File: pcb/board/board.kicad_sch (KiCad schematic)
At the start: 31 parts, among them J1 USB_C_Receptacle_USB2.0_14P, J2 Conn_01x03, SW1 SW_Push, U1 RP2040, U2 NCP1117-3.3_SOT223, U3 W25Q128JVS, Y1 12MHz

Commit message: 08012026 - tons of schematic work!
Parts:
- added C18, C19: 10uF, symbol Device:C
- added C20, C25: 1uF, symbol Device:C
- added C21, C22: 15uF, symbol Device:C
- added C23, C24, C26, C27, C28, C29, C30, C31, C32, C33, C34: 0.1uF, symbol Device:C
- added D1, D2: D, symbol Device:D
- added J3: (B) USB_C_Receptacle_USB2.0_14P, symbol Connector:USB_C_Receptacle_USB2.0_14P
- added J4: (C) USB_C_Receptacle_USB2.0_14P, symbol Connector:USB_C_Receptacle_USB2.0_14P
- added J5: Conn_01x03, symbol Connector_Generic:Conn_01x03
- added R10, R11, R8, R9: 5.1K, symbol Device:R
- added R12, R13: 27, symbol Device:R
- added R14, R16: 1K, symbol Device:R
- added R15: 10K, symbol Device:R
- added SW2: SW_Push, symbol Switch:SW_Push
- added U4: NCP1117-3.3_SOT223, Package_TO_SOT_SMD:SOT-223-3_TabPin2, symbol Regulator_Linear:NCP1117-3.3_SOT223
- added U5: RP2040, Package_DFN_QFN:QFN-56-1EP_7x7mm_P0.4mm_EP3.2x3.2mm, symbol MCU_RaspberryPi:RP2040
- added U6: W25Q128JVS, Package_SO:SOIC-8_5.23x5.23mm_P1.27mm, symbol Memory_Flash:W25Q128JVS
- added Y2: 12MHz, symbol Device:Crystal_GND24
- J1: value USB_C_Receptacle_USB2.0_14P -> (A) USB_C_Receptacle_USB2.0_14P
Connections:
- net GND: now also C18.2, C19.2, C20.2, C21.1, C22.1, C23.2, C24.2, C25.2, C26.2, C27.2, C28.2, C29.2, C30.2, C31.2, C32.2, C33.2, C34.2, J3.A1 (GND), J3.A12 (GND), J3.B1 (GND), J3.B12 (GND), J3.S1 (SHIELD), J4.A1 (GND), J4.A12 (GND), J4.B1 (GND), J4.B12 (GND), J4.S1 (SHIELD), J5.2 (Pin_2), R10.2, R11.1, R8.2, R9.1, SW2.1, U4.1 (GND), U5.19 (TESTEN), U5.57 (GND), U6.4 (GND), Y2.2, Y2.4
- net +1V1 renamed +1V1_A
- net +3V3 renamed +3V3_A
- net QSPI_SCLK renamed QSPI_SCLK_A
- net QSPI_SD0 renamed QSPI_SD0_A
- net QSPI_SD1 renamed QSPI_SD1_A
- net QSPI_SD2 renamed QSPI_SD2_A
- net QSPI_SD3 renamed QSPI_SD3_A
- net QSPI_SS renamed QSPI_SS_A
- net RUN renamed RUN_A
- net SWCLK renamed SWCLK_A
- net SWD renamed SWD_A
- net USB D+ renamed USB_A D+
- net USB D- renamed USB_A D-
- net VBUS renamed VBUS_A
- net VBUS_A: now also D1.1 (K)
- net XIN renamed XIN_A
- net XOUT renamed XOUT_A
- new net: D1.2 (A), D2.2 (A), J4.A4 (VBUS), J4.A9 (VBUS), J4.B4 (VBUS), J4.B9 (VBUS)
- new net: C22.2, R16.1, Y2.1
- new net: J4.A5 (CC1), R10.1
- new net: J4.B5 (CC2), R11.2
- new net: R14.1, SW2.2
- new net: J3.A5 (CC1), R8.1
- new net: R13.1, U5.46 (USB_DM)
- new net: R12.2, U5.47 (USB_DP)
- new net: J3.B5 (CC2), R9.2
- new net +1V1_B: C20.1, C23.1, C24.1, U5.23 (DVDD), U5.45 (VREG_VOUT), U5.50 (DVDD)
- new net +3V3_B: C19.1, C25.1, C26.1, C27.1, C28.1, C29.1, C30.1, C31.1, C32.1, C33.1, C34.1, R15.1, U4.2 (VO), U5.1 (IOVDD), U5.10 (IOVDD), U5.22 (IOVDD), U5.33 (IOVDD), U5.42 (IOVDD), U5.43 (ADC_AVDD), U5.44 (VREG_IN), U5.48 (USB_VDD), U5.49 (IOVDD), U6.8 (VCC)
- new net QSPI_SCLK_B: U5.52 (QSPI_SCLK), U6.6 (CLK)
- new net QSPI_SD0_B: U5.53 (QSPI_SD0), U6.5 (DI(IO0))
- new net QSPI_SD1_B: U5.55 (QSPI_SD1), U6.2 (DO(IO1))
- new net QSPI_SD2_B: U5.54 (QSPI_SD2), U6.3 (IO2)
- new net QSPI_SD3_B: U5.51 (QSPI_SD3), U6.7 (IO3)
- new net QSPI_SS_B: R14.2, R15.2, U5.56 (QSPI_SS), U6.1 (~{CS})
- new net RUN_B: U5.26 (RUN)
- new net SWCLK_B: J5.1 (Pin_1), U5.24 (SWCLK)
- new net SWD_B: J5.3 (Pin_3), U5.25 (SWD)
- new net USB_B D+: J3.A6 (D+), J3.B6 (D+), R12.1
- new net USB_B D-: J3.A7 (D-), J3.B7 (D-), R13.2
- new net VBUS_B: C18.1, D2.1 (K), J3.A4 (VBUS), J3.A9 (VBUS), J3.B4 (VBUS), J3.B9 (VBUS), U4.3 (VI)
- new net XIN_B: C21.2, U5.20 (XIN), Y2.3
- new net XOUT_B: R16.2, U5.21 (XOUT)
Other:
- note added: "TODO: NEED TO SELECT DIODES!!!"
- moved on the sheet: C1, C10, C11, C12, C13, C14, C15, C16, C17, C2, C3, C4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

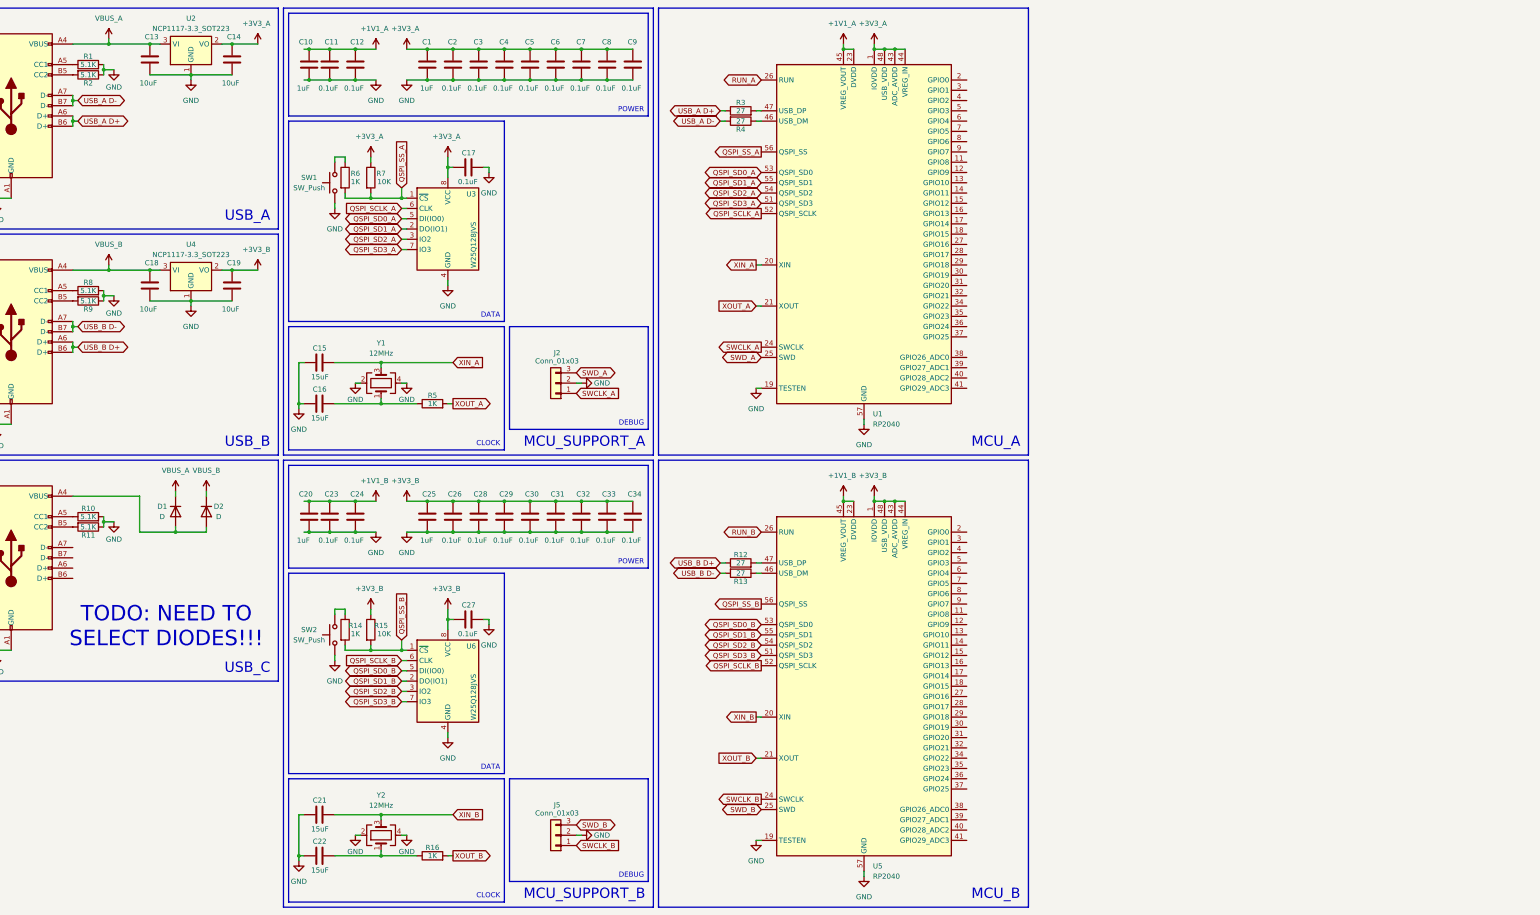
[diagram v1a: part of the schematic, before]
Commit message: add connector pins to the schematic!
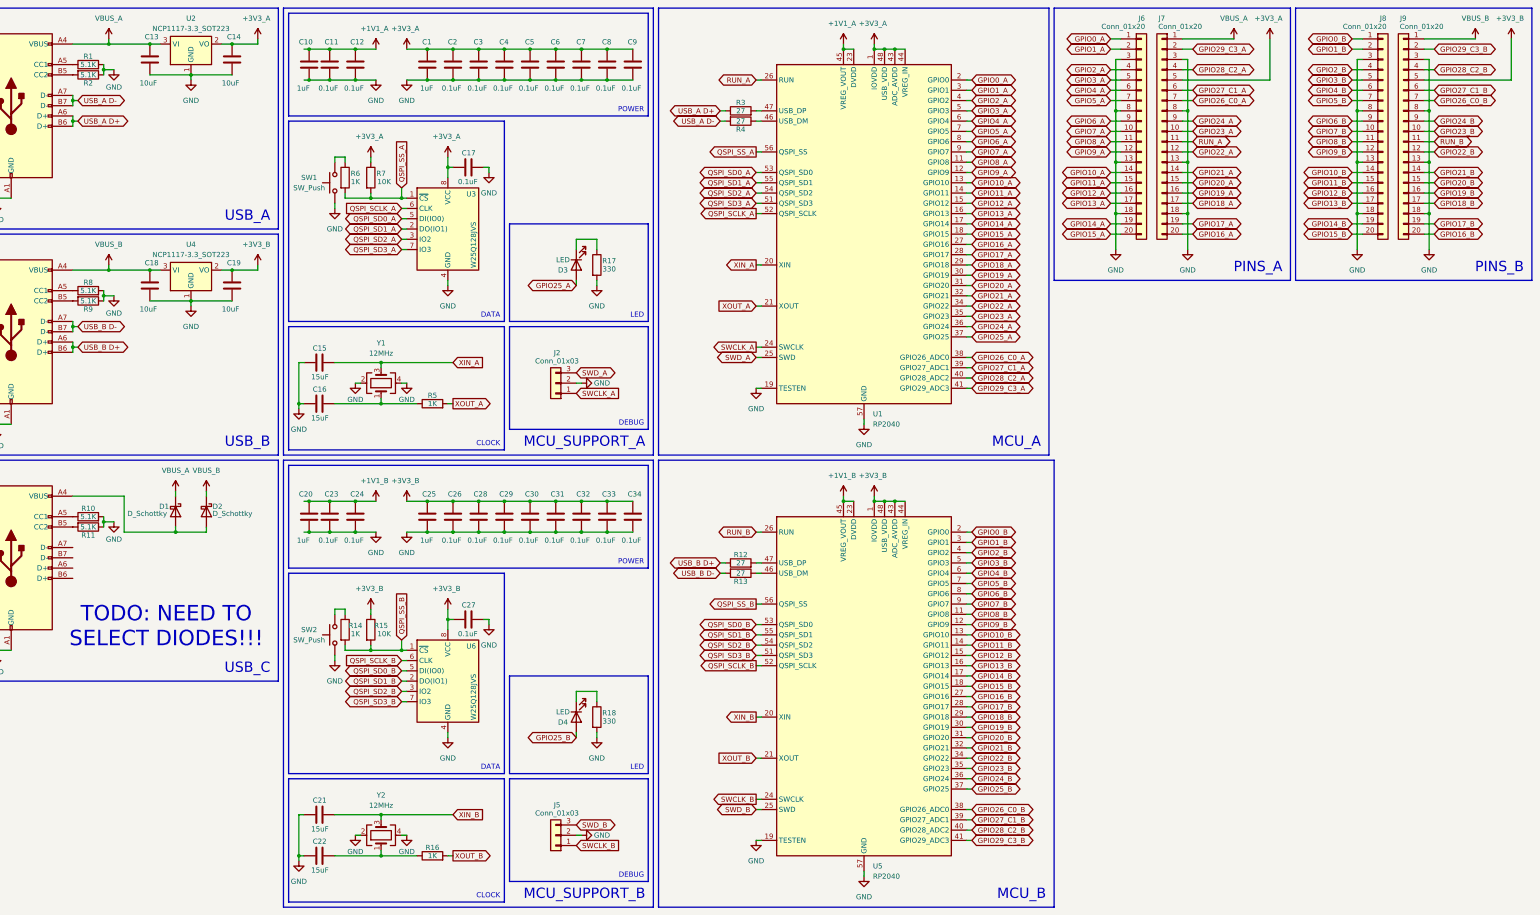
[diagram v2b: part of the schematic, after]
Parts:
- removed D1, D2: D, symbol Device:D
- added D1, D2: D_Schottky, symbol Device:D_Schottky
- added D3, D4: LED, symbol Device:LED
- added J6, J7, J8, J9: Conn_01x20, symbol Connector_Generic:Conn_01x20
- added R17, R18: 330, symbol Device:R
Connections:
- net +3V3_A: now also J7.5 (Pin_5)
- net +3V3_B: now also J9.5 (Pin_5)
- net GND: now also J6.13 (Pin_13), J6.18 (Pin_18), J6.3 (Pin_3), J6.8 (Pin_8), J7.13 (Pin_13), J7.18 (Pin_18), J7.3 (Pin_3), J7.8 (Pin_8), J8.13 (Pin_13), J8.18 (Pin_18), J8.3 (Pin_3), J8.8 (Pin_8), J9.13 (Pin_13), J9.18 (Pin_18), J9.3 (Pin_3), J9.8 (Pin_8), R17.2, R18.2
- net RUN_A: now also J7.11 (Pin_11)
- net RUN_B: now also J9.11 (Pin_11)
- net VBUS_A: now also D1.1 (K), J7.1 (Pin_1)
- net VBUS_B: now also D2.1 (K), J9.1 (Pin_1)
- net at J4.A4 (VBUS), J4.A9 (VBUS), J4.B4 (VBUS)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: now also D1.2 (A), D2.2 (A)
- net GPIO8_B: now reaches U5.11 (GPIO8)
- net GPIO8_B: now also J8.11 (Pin_11)
- net GPIO9_B: now reaches U5.12 (GPIO9)
- net GPIO9_B: now also J8.12 (Pin_12)
- net GPIO10_B: now reaches U5.13 (GPIO10)
- net GPIO10_B: now also J8.14 (Pin_14)
- net GPIO11_B: now reaches U5.14 (GPIO11)
- net GPIO11_B: now also J8.15 (Pin_15)
- net GPIO12_B: now reaches U5.15 (GPIO12)
- net GPIO12_B: now also J8.16 (Pin_16)
- net GPIO13_B: now reaches U5.16 (GPIO13)
- net GPIO13_B: now also J8.17 (Pin_17)
- net GPIO14_B: now reaches U5.17 (GPIO14)
- net GPIO14_B: now also J8.19 (Pin_19)
- net GPIO15_B: now reaches U5.18 (GPIO15)
- net GPIO15_B: now also J8.20 (Pin_20)
- net GPIO0_B: now reaches U5.2 (GPIO0)
- net GPIO0_B: now also J8.1 (Pin_1)
- net GPIO16_B: now reaches U5.27 (GPIO16)
- net GPIO16_B: now also J9.20 (Pin_20)
- net GPIO17_B: now reaches U5.28 (GPIO17)
- net GPIO17_B: now also J9.19 (Pin_19)
- net GPIO18_B: now reaches U5.29 (GPIO18)
- net GPIO18_B: now also J9.17 (Pin_17)
- net GPIO1_B: now reaches U5.3 (GPIO1)
- net GPIO1_B: now also J8.2 (Pin_2)
- net GPIO19_B: now reaches U5.30 (GPIO19)
- net GPIO19_B: now also J9.16 (Pin_16)
- net GPIO20_B: now reaches U5.31 (GPIO20)
- net GPIO20_B: now also J9.15 (Pin_15)
- net GPIO21_B: now reaches U5.32 (GPIO21)
- net GPIO21_B: now also J9.14 (Pin_14)
- net GPIO22_B: now reaches U5.34 (GPIO22)
- net GPIO22_B: now also J9.12 (Pin_12)
- net GPIO23_B: now reaches U5.35 (GPIO23)
- net GPIO23_B: now also J9.10 (Pin_10)
- net GPIO24_B: now reaches U5.36 (GPIO24)
- net GPIO24_B: now also J9.9 (Pin_9)
- net GPIO25_B: now reaches U5.37 (GPIO25)
- net GPIO25_B: now also D4.2 (A)
- net GPIO26_C0_B: now reaches U5.38 (GPIO26_ADC0)
- net GPIO26_C0_B: now also J9.7 (Pin_7)
- net GPIO27_C1_B: now reaches U5.39 (GPIO27_ADC1)
- net GPIO27_C1_B: now also J9.6 (Pin_6)
- net GPIO2_B: now reaches U5.4 (GPIO2)
- net GPIO2_B: now also J8.4 (Pin_4)
- net GPIO28_C2_B: now reaches U5.40 (GPIO28_ADC2)
- net GPIO28_C2_B: now also J9.4 (Pin_4)
- net GPIO29_C3_B: now reaches U5.41 (GPIO29_ADC3)
- net GPIO29_C3_B: now also J9.2 (Pin_2)
- net GPIO3_B: now reaches U5.5 (GPIO3)
- net GPIO3_B: now also J8.5 (Pin_5)
- net GPIO4_B: now reaches U5.6 (GPIO4)
- net GPIO4_B: now also J8.6 (Pin_6)
- net GPIO5_B: now reaches U5.7 (GPIO5)
- net GPIO5_B: now also J8.7 (Pin_7)
- net GPIO6_B: now reaches U5.8 (GPIO6)
- net GPIO6_B: now also J8.9 (Pin_9)
- net GPIO7_B: now reaches U5.9 (GPIO7)
- net GPIO7_B: now also J8.10 (Pin_10)
- net GPIO8_A: now reaches U1.11 (GPIO8)
- net GPIO8_A: now also J6.11 (Pin_11)
- net GPIO9_A: now reaches U1.12 (GPIO9)
- net GPIO9_A: now also J6.12 (Pin_12)
- net GPIO10_A: now reaches U1.13 (GPIO10)
- net GPIO10_A: now also J6.14 (Pin_14)
- net GPIO11_A: now reaches U1.14 (GPIO11)
- net GPIO11_A: now also J6.15 (Pin_15)
- net GPIO12_A: now reaches U1.15 (GPIO12)
- net GPIO12_A: now also J6.16 (Pin_16)
- net GPIO13_A: now reaches U1.16 (GPIO13)
- net GPIO13_A: now also J6.17 (Pin_17)
- net GPIO14_A: now reaches U1.17 (GPIO14)
- net GPIO14_A: now also J6.19 (Pin_19)
- net GPIO15_A: now reaches U1.18 (GPIO15)
- net GPIO15_A: now also J6.20 (Pin_20)
- net GPIO0_A: now reaches U1.2 (GPIO0)
- net GPIO0_A: now also J6.1 (Pin_1)
- net GPIO16_A: now reaches U1.27 (GPIO16)
- net GPIO16_A: now also J7.20 (Pin_20)
- net GPIO17_A: now reaches U1.28 (GPIO17)
- net GPIO17_A: now also J7.19 (Pin_19)
- net GPIO18_A: now reaches U1.29 (GPIO18)
- net GPIO18_A: now also J7.17 (Pin_17)
- net GPIO1_A: now reaches U1.3 (GPIO1)
- net GPIO1_A: now also J6.2 (Pin_2)
- net GPIO19_A: now reaches U1.30 (GPIO19)
- net GPIO19_A: now also J7.16 (Pin_16)
- net GPIO20_A: now reaches U1.31 (GPIO20)
- net GPIO20_A: now also J7.15 (Pin_15)
- net GPIO21_A: now reaches U1.32 (GPIO21)
- net GPIO21_A: now also J7.14 (Pin_14)
- net GPIO22_A: now reaches U1.34 (GPIO22)
- net GPIO22_A: now also J7.12 (Pin_12)
- net GPIO23_A: now reaches U1.35 (GPIO23)
- net GPIO23_A: now also J7.10 (Pin_10)
- net GPIO24_A: now reaches U1.36 (GPIO24)
- net GPIO24_A: now also J7.9 (Pin_9)
- net GPIO25_A: now reaches U1.37 (GPIO25)
- net GPIO25_A: now also D3.2 (A)
- net GPIO26_C0_A: now reaches U1.38 (GPIO26_ADC0)
- net GPIO26_C0_A: now also J7.7 (Pin_7)
- net GPIO27_C1_A: now reaches U1.39 (GPIO27_ADC1)
- net GPIO27_C1_A: now also J7.6 (Pin_6)
- net GPIO2_A: now reaches U1.4 (GPIO2)
- net GPIO2_A: now also J6.4 (Pin_4)
- net GPIO28_C2_A: now reaches U1.40 (GPIO28_ADC2)
- net GPIO28_C2_A: now also J7.4 (Pin_4)
- net GPIO29_C3_A: now reaches U1.41 (GPIO29_ADC3)
- net GPIO29_C3_A: now also J7.2 (Pin_2)
- net GPIO3_A: now reaches U1.5 (GPIO3)
- net GPIO3_A: now also J6.5 (Pin_5)
- net GPIO4_A: now reaches U1.6 (GPIO4)
- net GPIO4_A: now also J6.6 (Pin_6)
- net GPIO5_A: now reaches U1.7 (GPIO5)
- net GPIO5_A: now also J6.7 (Pin_7)
- net GPIO6_A: now reaches U1.8 (GPIO6)
- net GPIO6_A: now also J6.9 (Pin_9)
- net GPIO7_A: now reaches U1.9 (GPIO7)
- net GPIO7_A: now also J6.10 (Pin_10)
- new net: D4.1 (K), R18.1
- new net: D3.1 (K), R17.1

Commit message: add display footprint/symbol and switches/encoder wiring!
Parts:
- added D5, D6, D7, D8: Diode, symbol ScottoKeebs:Placeholder_Diode
- added J10: OLED_128x32, ScottoKeebs_Components:OLED_128x32, symbol ScottoKeebs:OLED_128x32
- added J11: LCD_128x160, Library:LCD_128x160, symbol Library:LCD_128x160
- added J12: Conn_01x03, Connector_PinHeader_2.54mm:PinHeader_1x03_P2.54mm_Vertical, symbol Connector_Generic:Conn_01x03
- added SW3, SW4, SW5: Switch, symbol ScottoKeebs:Placeholder_Switch
- added SW6: RotaryEncoder_Switch, Rotary_Encoder:RotaryEncoder_Alps_EC11E_Vertical_H20mm, symbol Device:RotaryEncoder_Switch
- C1, C10, C11, C12, C13, C14, C15, C16, C17, C18, C19, C2, C20, C21, C22, C23, C24, C25, C26, C27, C28, C29, C3, C30, C31, C32, C33, C34, C4, C5, C6, C7, C8, C9: footprint (none) -> Capacitor_SMD:C_0402_1005Metric
- J1: footprint (none) -> Connector_USB:USB_C_Receptacle_HRO_TYPE-C-31-M-12
- J2: renamed from J3; footprint (none) -> Connector_USB:USB_C_Receptacle_HRO_TYPE-C-31-M-12
- J3: renamed from J4; footprint (none) -> Connector_USB:USB_C_Receptacle_HRO_TYPE-C-31-M-12
- J4: renamed from J2; footprint (none) -> Connector_PinHeader_2.54mm:PinHeader_1x03_P2.54mm_Vertical
- J5: footprint (none) -> Connector_PinHeader_2.54mm:PinHeader_1x03_P2.54mm_Vertical
- J6, J7, J8, J9: footprint (none) -> Connector_PinHeader_2.54mm:PinHeader_1x20_P2.54mm_Vertical
- R1, R10, R11, R12, R13, R14, R15, R16, R17, R18, R2, R3, R4, R5, R6, R7, R8, R9: footprint (none) -> Resistor_SMD:R_0402_1005Metric
- SW1, SW2: footprint (none) -> Button_Switch_SMD:SW_Push_SPST_NO_Alps_SKRK
- Y1, Y2: footprint (none) -> Crystal:Crystal_SMD_3225-4Pin_3.2x2.5mm
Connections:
- net GND: now also J10.1 (GND), J11.1 (GND), J12.3 (Pin_3), SW6.C
- net GPIO0_A: now also J12.1 (Pin_1)
- net GPIO1_A: now also SW3.1
- net GPIO2_A: now also SW4.1
- net GPIO3_A: now also SW5.1
- net GPIO4_A: now also SW6.S1
- net GPIO5_A: now also SW6.A
- net GPIO6_A: now also SW6.B
- new net: D5.1 (K), D6.1 (K), D7.1 (K), D8.1 (K), J12.2 (Pin_2)
- new net: D7.2 (A), SW5.2
- new net: D6.2 (A), SW4.2
- new net: D5.2 (A), SW3.2
- new net: D8.2 (A), SW6.S2
- no-connect marks 0 -> 4
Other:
- note added: "TODO: ADD AUDIO JACK WIRING!!!"

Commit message: 08022026 - more schematic work!
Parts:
- D5, D6, D7, D8: footprint (none) -> Diode_THT:D_DO-35_SOD27_P7.62mm_Horizontal
- SW3, SW4, SW5: footprint (none) -> Button_Switch_Keyboard:SW_Cherry_MX_1.00u_PCB
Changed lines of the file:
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@@
 	(text_box "INTERACTION"
 		(exclude_from_sim no)
-		(at 424.18 85.09 0)
+		(at 287.02 83.82 0)
 		(size 118.11 153.67)
 		(stroke
@@
 		)
 	)
+	(text_box "DISPLAYS"
+		(exclude_from_sim no)
+		(at 288.29 85.09 0)
+		(size 57.15 82.55)
+		(stroke
+			(width 0)
+			(type default)
+		)
+		(fill
+			(type none)
+		)
+		(effects
+			(font
+				(size 2.54 2.54)
+			)
+			(justify right bottom)
+		)
+	)
 	(text_box "PINS_A"
 		(exclude_from_sim no)
@@
 	(text "TODO: ADD AUDIO\nJACK WIRING!!!"
 		(exclude_from_sim no)
-		(at 347.218 183.642 0)
+		(at 345.948 202.184 0)
 		(effects
 			(font
@@
 			)
 		)
-		(property "Footprint" ""
+		(property "Footprint" "Diode_THT:D_DO-35_SOD27_P7.62mm_Horizontal"
 			(at 386.08 120.65 0)
 			(effects
@@
 			)
 		)
-		(property "Footprint" ""
+		(property "Footprint" "Diode_THT:D_DO-35_SOD27_P7.62mm_Horizontal"
 			(at 386.08 110.49 0)
 			(effects
@@
 			)
 		)
-		(property "Footprint" ""
+		(property "Footprint" "Button_Switch_Keyboard:SW_Cherry_MX_1.00u_PCB"
 			(at 375.92 105.41 0)
 			(effects
@@
 			)
 		)
-		(property "Footprint" ""
+		(property "Footprint" "Button_Switch_Keyboard:SW_Cherry_MX_1.00u_PCB"
 			(at 375.92 95.25 0)
 			(effects
@@
 			)
 		)
-		(property "Footprint" ""
+		(property "Footprint" "Diode_THT:D_DO-35_SOD27_P7.62mm_Horizontal"
 			(at 391.16 135.89 0)
 			(effects
@@
 			)
 		)
-		(property "Footprint" ""
+		(property "Footprint" "Button_Switch_Keyboard:SW_Cherry_MX_1.00u_PCB"
 			(at 375.92 115.57 0)
 			(effects
@@
 			)
 		)
-		(property "Footprint" ""
+		(property "Footprint" "Diode_THT:D_DO-35_SOD27_P7.62mm_Horizontal"
 			(at 386.08 100.33 0)
 			(effects

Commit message: add audio and sd card stuff
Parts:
- added C35, C37, C39, C48: 10uF, Capacitor_SMD:C_0402_1005Metric, symbol Device:C
- added C36, C38, C40, C43: 100nF, Capacitor_SMD:C_0402_1005Metric, symbol Device:C
- added C41, C42, C44, C45: 2.2uF, Capacitor_SMD:C_0402_1005Metric, symbol Device:C
- added C46, C47: 1uF, Capacitor_SMD:C_0402_1005Metric, symbol Device:C
- added J13: AudioJack3, symbol Connector_Audio:AudioJack3
- added J14: Micro_SD_Card, symbol Connector:Micro_SD_Card
- added R19, R20: 470, Resistor_SMD:R_0402_1005Metric, symbol Device:R
- added R21: DNF, Resistor_SMD:R_0402_1005Metric, symbol Device:R
- added U7: PCM5101A, Package_SO:TSSOP-20_4.4x6.5mm_P0.65mm, symbol Audio:PCM5101A
- added U8: TLV70033_SOT23-5, Package_TO_SOT_SMD:SOT-23-5, symbol Regulator_Linear:TLV70033_SOT23-5
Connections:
- net +3V3_A: now also C39.1, C40.1, C48.1, J14.4 (VDD), U7.17 (XSMT), U7.20 (DVDD)
- net GND: now also C35.2, C36.2, C37.2, C38.2, C39.2, C40.2, C42.2, C43.2, C44.2, C45.2, C46.2, C47.2, C48.2, J13.S, J14.6 (VSS), J14.9 (SHIELD), R21.2, U7.10 (DEMP), U7.11 (FLT), U7.12 (SCK), U7.16 (FMT), U7.19 (DGND), U7.3 (CPGND), U7.9 (AGND), U8.2 (GND)
- net GPIO10_A: now also J14.5 (CLK), R21.1
- net GPIO11_A: now also J14.3 (CMD)
- net GPIO26_C0_A: now also U7.14 (DIN)
- net GPIO27_C1_A: now also U7.13 (BCK)
- net GPIO28_C2_A: now also U7.15 (LRCK)
- net GPIO8_A: now also J14.7 (DAT0)
- net GPIO9_A: now also J14.2 (DAT3/CD)
- net VBUS_A: now also C46.1, U8.1 (IN), U8.3 (EN)
- new net: R19.1, U7.6 (OUTL)
- new net: C45.1, J13.T, R19.2
- new net: R20.1, U7.7 (OUTR)
- new net: C44.1, J13.R, R20.2
- new net: C43.1, U7.18 (LDOO)
- new net: C41.1, U7.2 (CAPP)
- new net: C41.2, U7.4 (CAPM)
- new net: C42.1, U7.5 (VNEG)
- new net +3V3_AUDIO: C35.1, C36.1, C37.1, C38.1, C47.1, U7.1 (CPVDD), U7.8 (AVDD), U8.5 (OUT)
- no-connect marks 4 -> 6
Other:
- note added: "0-6: Buttons 8-11: SD Card 26-28: Audio"
- note added: "SPI Interface DAT0-RX-MISO (8) CMD-TX-MOSI (11) DAT3-CS (9) CLK-SCK(10)"
- note removed: "TODO: ADD AUDIO JACK WIRING!!!"
- moved on the sheet: C10, D5, D6, D7, D8, J10, J11, J12, SW3, SW4, SW5, SW6

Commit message: add labels for display pins (and added leds!)
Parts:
- added D10, D9: LED, symbol Device:LED
- added D11, D12, D13, D14, D15, D16: LED_WS2812B, ScottoKeebs_Components:LED_WS2812B, symbol ScottoKeebs:LED_WS2812B
- added R22, R23: 330, Resistor_SMD:R_0402_1005Metric, symbol Device:R
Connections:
- net +3V3_A: now also J10.2 (VCC), D11.1 (VDD), D12.1 (VDD), D13.1 (VDD)
- net +3V3_B: now also J11.2 (VCC), D14.1 (VDD), D15.1 (VDD), D16.1 (VDD)
- net GND: now also D11.3 (VSS), D12.3 (VSS), D13.3 (VSS), D14.3 (VSS), D15.3 (VSS), D16.3 (VSS), R22.2, R23.2
- net GPIO0_B: now also J11.6 (DC)
- net GPIO12_A: now also J10.4 (SDA)
- net GPIO13_A: now also J10.3 (SCL)
- net GPIO1_B: now also J11.7 (CS)
- net GPIO23_A: now also D11.4 (DIN)
- net GPIO23_B: now also D14.4 (DIN)
- net GPIO24_A: now also D9.2 (A)
- net GPIO24_B: now also D10.2 (A)
- net GPIO2_B: now also J11.3 (SCL)
- net GPIO3_B: now also J11.4 (SDA)
- net GPIO4_B: now also J11.5 (RST)
- net GPIO5_B: now also J11.8 (BLK)
- new net: D11.2 (DOUT), D12.4 (DIN)
- new net: D9.1 (K), R22.1
- new net: D15.2 (DOUT), D16.4 (DIN)
- new net: D10.1 (K), R23.1
- new net: D14.2 (DOUT), D15.4 (DIN)
- new net: D12.2 (DOUT), D13.4 (DIN)
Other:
- note added: "0-5: LCD 128x160 Display 23: RGB LEDS 24: Board LED 25: Boot LED"
- note added: "0-6: Buttons 8-11: Micro SD Card 12-13: OLED 128x32 Display 23: RGB LEDS 24: Board LED 25: Boot LED 26-28: Audio"
- note added: "GPIO12: I2C0 SDA GPIO13: I2C0 SCL"
- note added: "GPIO5: BLK, generic GPIO1: CS, SPI0 CSn GPIO0: DC, generic GPIO4: RST, generic GPIO3: SDA, SPI0 TX (MOSI) GPIO2: SCL, SPI0 SCK"
- note added: "TODO: DOUBLE CHECK 128X160 PINS!!!"
- note removed: "0-6: Buttons 8-11: SD Card 26-28: Audio"
- moved on the sheet: C46, J10, J11, U8
